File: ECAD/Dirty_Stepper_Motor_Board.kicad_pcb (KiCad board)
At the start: 4 copper layers, 41 x 35 mm, 24 parts, among them J1 PWR_IN, J2 MTR_CTRL_IN, J3 SPI, M1 17HS4412B, U1 DRV8461SPWP

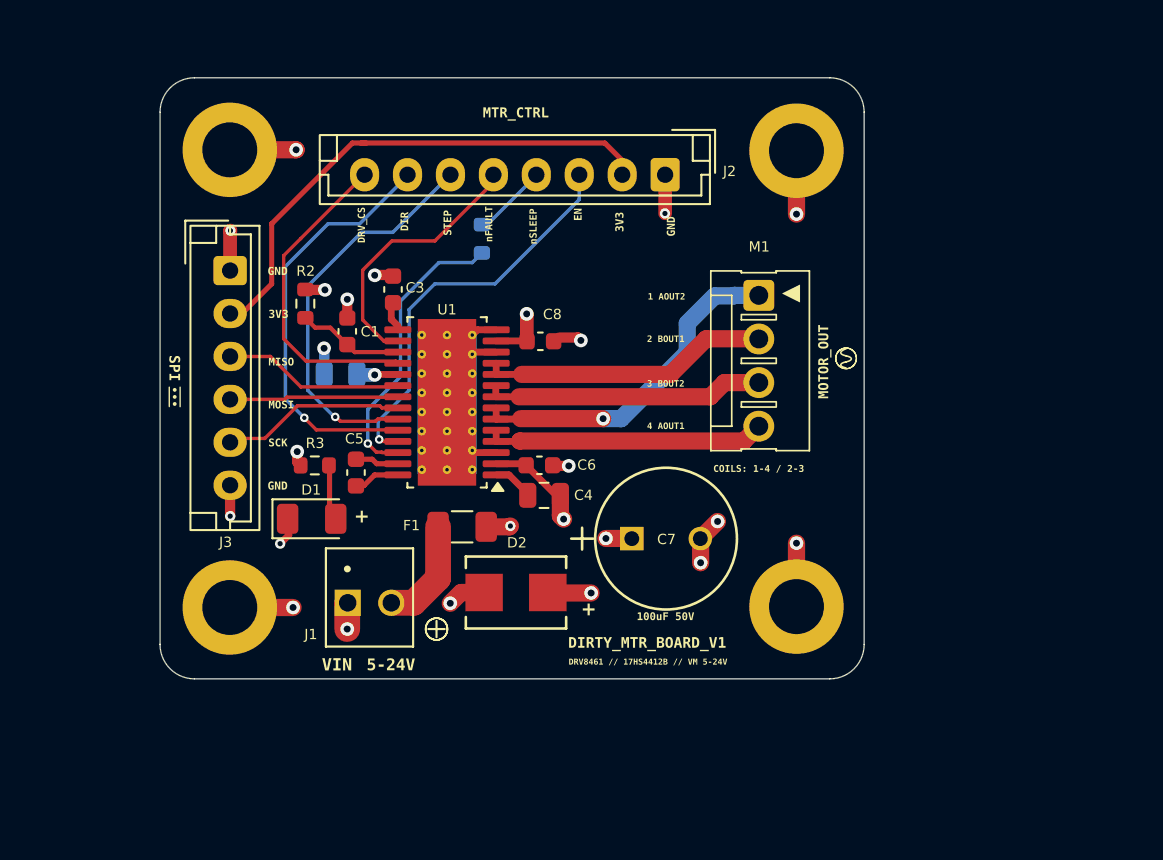
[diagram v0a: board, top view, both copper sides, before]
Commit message: Added stitching vias
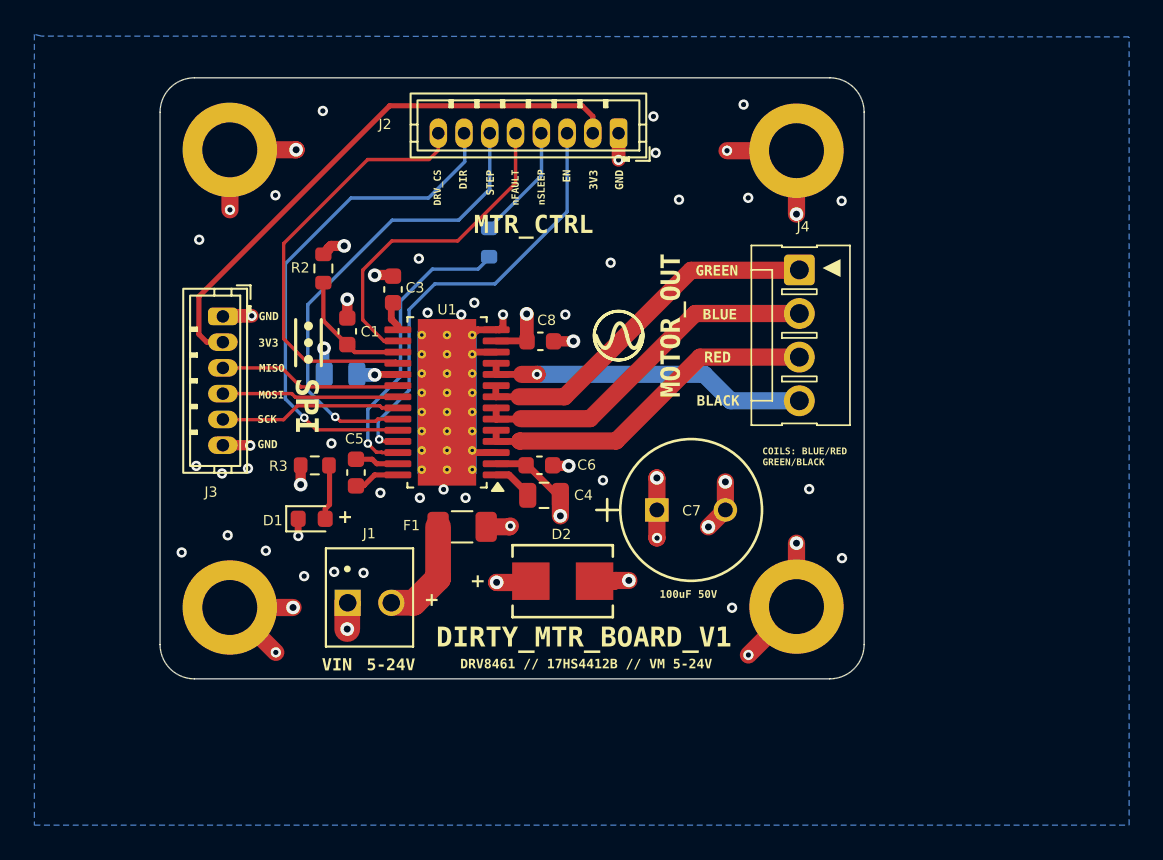
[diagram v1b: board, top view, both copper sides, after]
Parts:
- removed M1: 17HS4412B, MTA:MTA-4
- removed REF**: ESD-Logo_8.9x8mm_SilkScreen, SILK_SCREEN:ESD-Logo_8.9x8mm_SilkScreen
- added J4: MTR1, MTA:MTA-4, F.Cu at (123.2, 124.3)
- D1: footprint LED:LED_1206_3216Metric -> LED:LED_0603_1608Metric
- J2: footprint JST_EH:JST_EH_B8B-EH-A_1x08_P2.50mm_Vertical -> JST_ZH:JST_ZH_B8B-ZR_1x08_P1.50mm_Vertical
- J3: footprint JST_EH:JST_EH_B6B-EH-A_1x06_P2.50mm_Vertical -> JST_ZH:JST_ZH_B6B-ZR_1x06_P1.50mm_Vertical
- moved J2 3.63 mm to (112.7, 106.2)
- moved D2 2.80 mm to (109.4, 132.3)
- moved J3 2.70 mm to (89.7, 116.9)
- moved R2 2.30 mm to (95.5, 114.1)
- moved C7 2.22 mm to (114.9, 128.2)
- moved R1 0.47 mm to (105.2, 112.6)
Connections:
- net /AOUT1 renamed /RED
- net /AOUT2 renamed /BLUE
- net /BOUT1 renamed /BLACK
- net /BOUT2 renamed /GREEN
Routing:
- net /VM: track 17.5 -> 85.5 mm, vias 7 -> 8
- net V-GND: track 72.8 -> 86.8 mm, vias 18 -> 56
- net /DRV_CS: track 18.7 -> 25.0 mm
- net /DIR: track 24.4 -> 29.8 mm
- net /GREEN: track 16.3 -> 21.4 mm
- net /nFAULT: track 14.6 -> 19.4 mm
- net /STEP: track 23.1 -> 27.7 mm
- net /RED: track 16.0 -> 20.1 mm
- net /nSLEEP: track 4.35 -> 6.81 mm
- net /BLACK: track 16.8 -> 19.0 mm, vias 0 -> 1
- net /EN: track 23.5 -> 25.6 mm
- net +3.3V: track 30.5 -> 32.6 mm
- net /VREF: track 6.22 -> 7.31 mm
- net /BLUE: track 19.6 -> 20.6 mm, vias 1 -> 0
- added copper zone on B.Cu, net V-GND
- removed copper zone on In2.Cu, net /VM
